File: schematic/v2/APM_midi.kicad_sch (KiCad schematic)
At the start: 3 parts, among them J21 USB_A

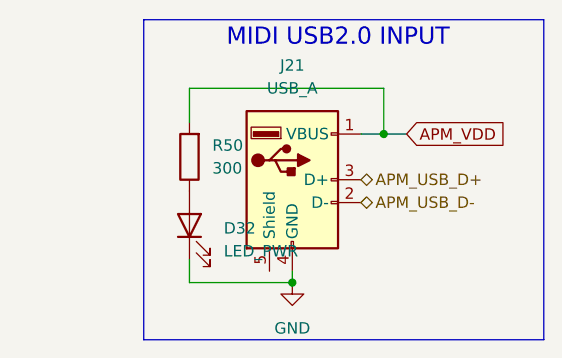
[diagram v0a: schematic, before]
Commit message: moving AAM -> APM. creatint some abstraction like stuff
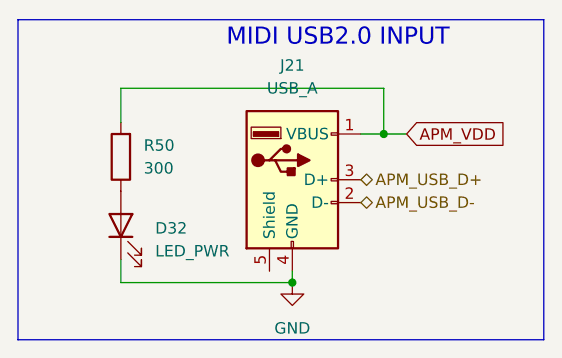
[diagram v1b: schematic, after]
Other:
- moved on the sheet: D32, R50
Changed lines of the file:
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@@
 	)
 	(rectangle
-		(start 121.92 80.01)
+		(start 107.95 80.01)
 		(end 166.37 115.57)
 		(stroke
@@
 	(wire
 		(pts
-			(xy 148.59 87.63) (xy 127 87.63)
+			(xy 148.59 87.63) (xy 119.38 87.63)
 		)
 		(stroke
@@
 	(wire
 		(pts
-			(xy 127 109.22) (xy 127 106.68)
+			(xy 119.38 109.22) (xy 119.38 106.68)
 		)
 		(stroke
@@
 	(wire
 		(pts
-			(xy 127 87.63) (xy 127 91.44)
+			(xy 119.38 87.63) (xy 119.38 91.44)
 		)
 		(stroke
@@
 	(wire
 		(pts
-			(xy 138.43 109.22) (xy 127 109.22)
+			(xy 138.43 109.22) (xy 119.38 109.22)
 		)
 		(stroke
@@
 	(symbol
 		(lib_id "Device:LED")
-		(at 127 102.87 90)
+		(at 119.38 102.87 90)
 		(unit 1)
 		(exclude_from_sim no)
@@
 		(fields_autoplaced yes)
 		(property "Reference" "D32"
-			(at 130.81 103.1874 90)
+			(at 123.19 103.1874 90)
 			(effects
 				(font
@@
 		)
 		(property "Value" "LED_PWR"
-			(at 130.81 105.7274 90)
+			(at 123.19 105.7274 90)
 			(effects
 				(font
@@
 		)
 		(property "Footprint" "LED_SMD:LED_0603_1608Metric"
-			(at 127 102.87 0)
+			(at 119.38 102.87 0)
 			(effects
 				(font
@@
 		)
 		(property "Datasheet" "~"
-			(at 127 102.87 0)
+			(at 119.38 102.87 0)
 			(effects
 				(font
@@
 		)
 		(property "Description" "Light emitting diode"
-			(at 127 102.87 0)
+			(at 119.38 102.87 0)
 			(effects
 				(font
@@
 		)
 		(property "Sim.Pins" "1=K 2=A"
-			(at 127 102.87 0)
+			(at 119.38 102.87 0)
 			(effects
 				(font
@@
 	(symbol
 		(lib_id "Device:R")
-		(at 127 95.25 180)
+		(at 119.38 95.25 180)
 		(unit 1)
 		(exclude_from_sim no)
@@
 		(fields_autoplaced yes)
 		(property "Reference" "R50"
-			(at 129.54 93.9799 0)
+			(at 121.92 93.9799 0)
 			(effects
 				(font
@@
 		)
 		(property "Value" "300"
-			(at 129.54 96.5199 0)
+			(at 121.92 96.5199 0)
 			(effects
 				(font
@@
 		)
 		(property "Footprint" "Resistor_SMD:R_0805_2012Metric_Pad1.20x1.40mm_HandSolder"
-			(at 128.778 95.25 90)
+			(at 121.158 95.25 90)
 			(effects
 				(font
@@
 		)
 		(property "Datasheet" "~"
-			(at 127 95.25 0)
+			(at 119.38 95.25 0)
 			(effects
 				(font
@@
 		)
 		(property "Description" "Resistor"
-			(at 127 95.25 0)
+			(at 119.38 95.25 0)
 			(effects
 				(font
@@
 		)
 		(property "DigiKey_Part_Number" "311-10.0KCRCT-ND"
-			(at 127 95.25 0)
+			(at 119.38 95.25 0)
 			(effects
 				(font
@@
 		)
 		(property "Price" "0.0129"
-			(at 127 95.25 0)
-			(effects
-				(font
+			(at 119.38 95.25 0)
+			(effects
+				(font

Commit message: no errors in the ERC!
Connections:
- no-connect marks 0 -> 1
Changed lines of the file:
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@@
 		(color 0 0 0 0)
 	)
+	(junction
+		(at 147.32 92.71)
+		(diameter 0)
+		(color 0 0 0 0)
+	)
+	(no_connect
+		(at 135.89 107.95)
+	)
 	(wire
 		(pts
@@
 	(wire
 		(pts
-			(xy 148.59 92.71) (xy 146.05 92.71)
+			(xy 148.59 92.71) (xy 147.32 92.71)
 		)
 		(stroke
@@
 		(pts
 			(xy 138.43 109.22) (xy 119.38 109.22)
+		)
+		(stroke
+			(width 0)
+			(type default)
+		)
+	)
+	(wire
+		(pts
+			(xy 147.32 92.71) (xy 146.05 92.71)
 		)
 		(stroke
@@
 					(unit 1)
 				)
+			)
+		)
+	)
+	(symbol
+		(lib_id "power:PWR_FLAG")
+		(at 147.32 92.71 180)
+		(unit 1)
+		(exclude_from_sim no)
+		(in_bom yes)
+		(on_board yes)
+		(dnp no)
+		(fields_autoplaced yes)
+		(property "Reference" "#FLG09"
+			(at 147.32 94.615 0)
+			(effects
+				(font
+					(size 1.27 1.27)
+				)
+				(hide yes)
+			)
+		)
+		(property "Value" "PWR_FLAG"
+			(at 147.32 97.79 0)
+			(effects
+				(font
+					(size 1.27 1.27)
+				)
+			)
+		)
+		(property "Footprint" ""
+			(at 147.32 92.71 0)
+			(effects
+				(font
+					(size 1.27 1.27)
+				)
+				(hide yes)
+			)
+		)
+		(property "Datasheet" "~"
+			(at 147.32 92.71 0)
+			(effects
+				(font
+					(size 1.27 1.27)
+				)
+				(hide yes)
+			)
+		)
+		(property "Description" "Special symbol for telling ERC where power comes from"
+			(at 147.32 92.71 0)
+			(effects
+				(font
+					(size 1.27 1.27)
+				)
+				(hide yes)
+			)
+		)
+		(pin "1"
+		)
+		(instances
+			(project ""
+				(path "/fe7b15e9-f0ed-4338-9f03-dd7651dace13/0125ec8c-bf97-4530-be23-1f3b075b267b/611fa31e-8b8a-419f-be1e-27301f4ddd3e"
+					(reference "#FLG09")
+					(unit 1)
+				)

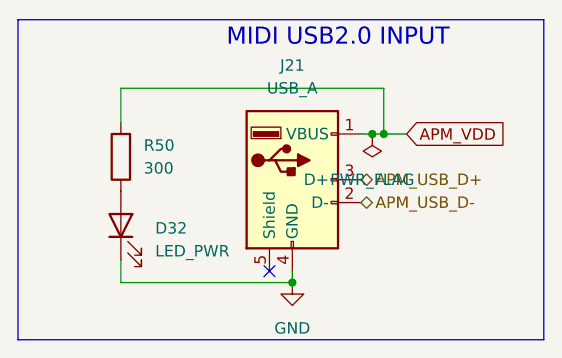
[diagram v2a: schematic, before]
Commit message: schematic updates, no errors at least. running DRC on pcb
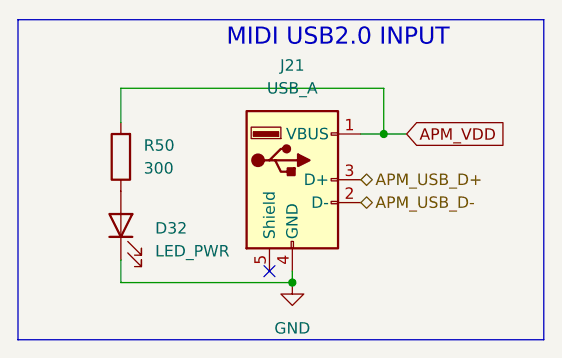
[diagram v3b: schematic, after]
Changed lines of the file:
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@@
-		(color 0 0 0 0)
-	)
-	(junction
-		(at 147.32 92.71)
-		(diameter 0)
 		(color 0 0 0 0)
 	)
@@
 	(wire
 		(pts
-			(xy 148.59 92.71) (xy 147.32 92.71)
-		)
-		(stroke
-			(width 0)
-			(type default)
-		)
-	)
-	(wire
-		(pts
 			(xy 148.59 92.71) (xy 151.13 92.71)
 		)
@@
 	(wire
 		(pts
-			(xy 147.32 92.71) (xy 146.05 92.71)
+			(xy 146.05 92.71) (xy 148.59 92.71)
 		)
 		(stroke
@@
 					(unit 1)
 				)
-			)
-		)
-	)
-	(symbol
-		(lib_id "power:PWR_FLAG")
-		(at 147.32 92.71 180)
-		(unit 1)
-		(exclude_from_sim no)
-		(in_bom yes)
-		(on_board yes)
-		(dnp no)
-		(fields_autoplaced yes)
-		(property "Reference" "#FLG09"
-			(at 147.32 94.615 0)
-			(effects
-				(font
-					(size 1.27 1.27)
-				)
-				(hide yes)
-			)
-		)
-		(property "Value" "PWR_FLAG"
-			(at 147.32 97.79 0)
-			(effects
-				(font
-					(size 1.27 1.27)
-				)
-			)
-		)
-		(property "Footprint" ""
-			(at 147.32 92.71 0)
-			(effects
-				(font
-					(size 1.27 1.27)
-				)
-				(hide yes)
-			)
-		)
-		(property "Datasheet" "~"
-			(at 147.32 92.71 0)
-			(effects
-				(font
-					(size 1.27 1.27)
-				)
-				(hide yes)
-			)
-		)
-		(property "Description" "Special symbol for telling ERC where power comes from"
-			(at 147.32 92.71 0)
-			(effects
-				(font
-					(size 1.27 1.27)
-				)
-				(hide yes)
-			)
-		)
-		(pin "1"
-		)
-		(instances
-			(project ""
-				(path "/fe7b15e9-f0ed-4338-9f03-dd7651dace13/0125ec8c-bf97-4530-be23-1f3b075b267b/611fa31e-8b8a-419f-be1e-27301f4ddd3e"
-					(reference "#FLG09")
-					(unit 1)
-				)
